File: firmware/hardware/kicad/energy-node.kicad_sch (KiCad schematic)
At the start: 14 parts, among them J1 MAINS 230V, J2 SCT-013-030 jack, J3 to Nucleo-F429ZI CN9/CN8, T1 ZMPT101B

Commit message: Update KiCad schematic and project files
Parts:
- J1: value MAINS 230V -> MAINS 230V AC
- J2: value SCT-013-030 jack -> SCT-013-030 JACK
- J3: value to Nucleo-F429ZI CN9/CN8 -> TO NUCLEO-F429ZI CN9/CN8
- R7: value 66.7 (internal) -> 66.7 internal
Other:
- note added: "1. VOLTAGE SENSING CHANNEL"
- note added: "2. CURRENT SENSING CHANNEL"
- note added: "230 V AC -> galvanic isolation and scaling -> anti-alias filter -> PA0 voltage ADC"
- note added: "3. SHARED ADC BIAS (MIDPOINT)"
- note added: "4. NUCLEO-F429ZI CONNECTIONS"
- note added: "Matching net labels connect signals without long crossing wires."
- note added: "PA0 = voltage samples; PA1 = current samples"
- note added: "Power-flag symbols are KiCad checks for supplied 3V3/GND; they are not physical parts."
- note added: "R2 converts the isolated transformer current into a measurable voltage."
- note added: "R3 and R4 make 1.65 V; C1 stabilizes it. This shifts both AC waveforms into the 0-3.3 V ADC range."
- note added: "R5 + C2 form a 1.6 kHz low-pass filter before the STM32 ADC."
- note added: "R6 + C3 match the voltage-channel filter so phase error stays aligned."
- note added: "R7 is the sensor's internal 66.7 ohm burden; do not add a second burden."
- note added: "SAFETY: J1 is mains voltage; use rated isolation, protection, and enclosure."
- note added: "SCT-013-030 clamp output -> internal burden -> anti-alias filter -> PA1 current ADC"
- note added: "V_BIAS = 1.65 V reference for both sensor channels"

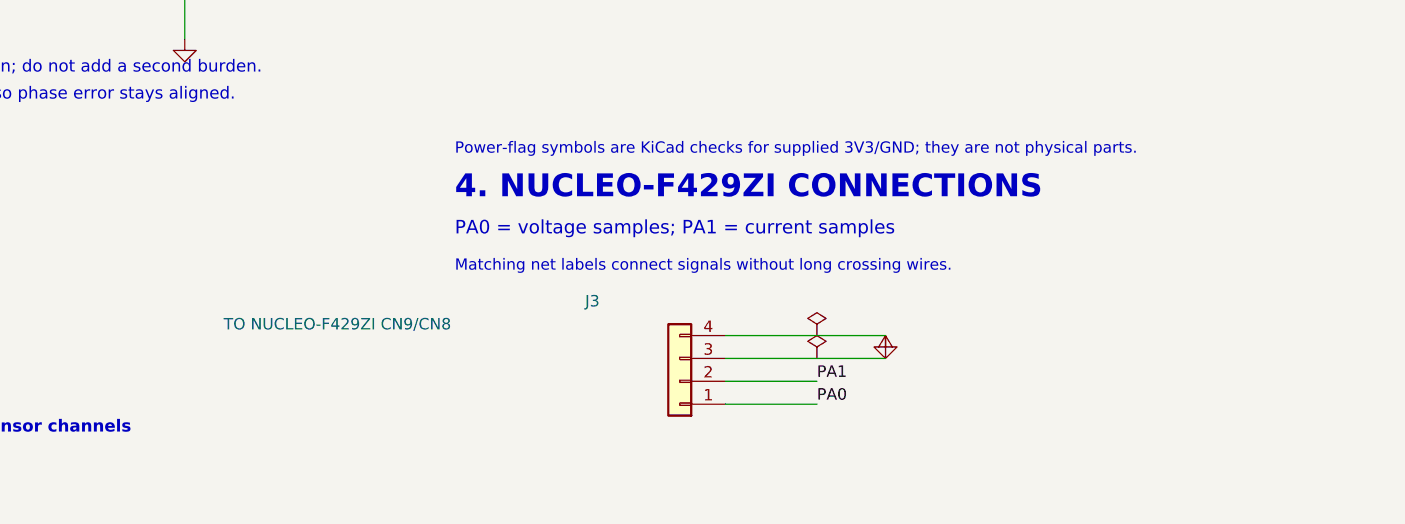
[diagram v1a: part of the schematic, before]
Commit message: Add explicit STM32 MCU model in schematic and docs
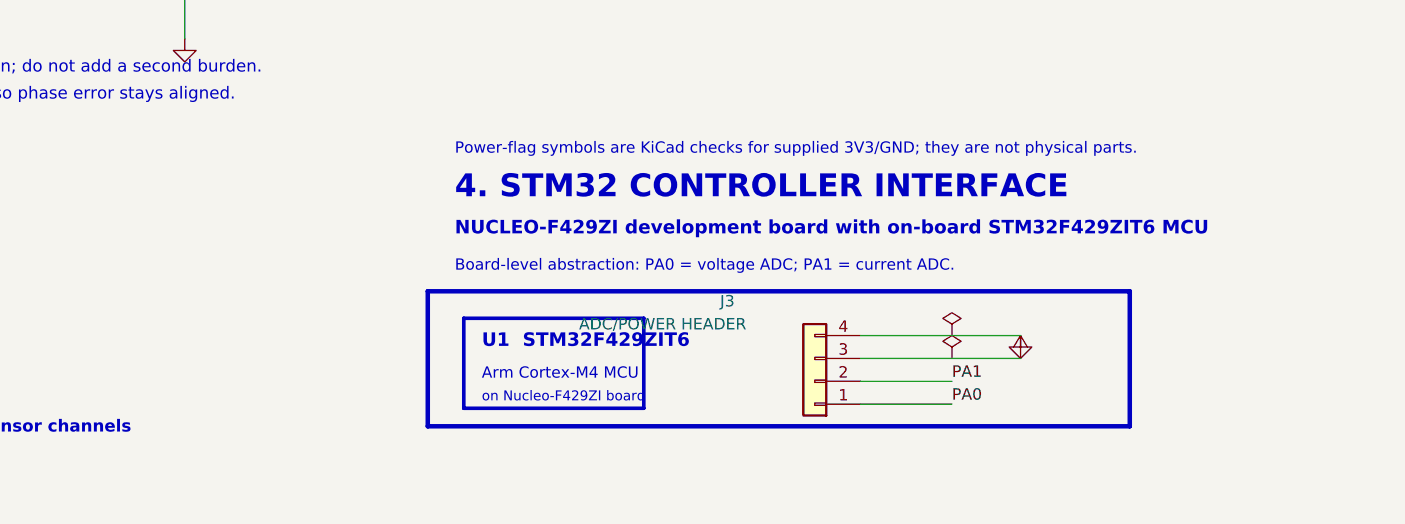
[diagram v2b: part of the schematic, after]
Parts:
- J3: value TO NUCLEO-F429ZI CN9/CN8 -> ADC/POWER HEADER
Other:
- note added: "4. STM32 CONTROLLER INTERFACE"
- note added: "Arm Cortex-M4 MCU"
- note added: "Board-level abstraction: PA0 = voltage ADC; PA1 = current ADC."
- note added: "NUCLEO-F429ZI development board with on-board STM32F429ZIT6 MCU"
- note added: "U1 STM32F429ZIT6"
- note added: "on Nucleo-F429ZI board"
- note removed: "4. NUCLEO-F429ZI CONNECTIONS"
- note removed: "Matching net labels connect signals without long crossing wires."
- note removed: "PA0 = voltage samples; PA1 = current samples"
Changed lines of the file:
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@@
   (wire (pts (xy 90 165.78) (xy 90 168.32)) (stroke (width 0) (type default)))
   (wire (pts (xy 90 158.16) (xy 110 158.16)) (stroke (width 0) (type default)))
-  (wire (pts (xy 225.08 159.54) (xy 235.24 159.54)) (stroke (width 0) (type default)))
-  (wire (pts (xy 225.08 157.0) (xy 235.24 157.0)) (stroke (width 0) (type default)))
-  (wire (pts (xy 225.08 154.46) (xy 242.86 154.46)) (stroke (width 0) (type default)))
-  (wire (pts (xy 225.08 151.92) (xy 242.86 151.92)) (stroke (width 0) (type default)))
+  (wire (pts (xy 240.08 159.54) (xy 250.24 159.54)) (stroke (width 0) (type default)))
+  (wire (pts (xy 240.08 157.0) (xy 250.24 157.0)) (stroke (width 0) (type default)))
+  (wire (pts (xy 240.08 154.46) (xy 257.86 154.46)) (stroke (width 0) (type default)))
+  (wire (pts (xy 240.08 151.92) (xy 257.86 151.92)) (stroke (width 0) (type default)))
   (label "PA0" (at 185 52.46 0) (fields_autoplaced) (effects (font (size 1.27 1.27)) (justify left bottom)))
   (junction (at 165 52.46) (diameter 0) (color 0 0 0 0))
@@
   (label "V_BIAS" (at 115.16 112.62 0) (fields_autoplaced) (effects (font (size 1.27 1.27)) (justify left bottom)))
   (label "V_BIAS" (at 110 158.16 0) (fields_autoplaced) (effects (font (size 1.27 1.27)) (justify left bottom)))
-  (label "PA0" (at 235.24 159.54 0) (fields_autoplaced) (effects (font (size 1.27 1.27)) (justify left bottom)))
-  (label "PA1" (at 235.24 157.0 0) (fields_autoplaced) (effects (font (size 1.27 1.27)) (justify left bottom)))
+  (label "PA0" (at 250.24 159.54 0) (fields_autoplaced) (effects (font (size 1.27 1.27)) (justify left bottom)))
+  (label "PA1" (at 250.24 157.0 0) (fields_autoplaced) (effects (font (size 1.27 1.27)) (justify left bottom)))
+  (rectangle (start 192 147) (end 270 162) (stroke (width 0.5) (type default)) (fill (type none)))
+  (rectangle (start 196 150) (end 216 160) (stroke (width 0.4) (type default)) (fill (type none)))
   (text "1. VOLTAGE SENSING CHANNEL" (at 25 30 0) (effects (font (size 2.54 2.54) bold) (justify left bottom)))
   (text "230 V AC -> galvanic isolation and scaling -> anti-alias filter -> PA0 voltage ADC" (at 25 34 0) (effects (font (size 1.6 1.6)) (justify left bottom)))
@@
   (text "V_BIAS = 1.65 V reference for both sensor channels" (at 105 163 0) (effects (font (size 1.35 1.35) bold) (justify left bottom)))
   (text "Power-flag symbols are KiCad checks for supplied 3V3/GND; they are not physical parts." (at 195 132 0) (effects (font (size 1.25 1.25)) (justify left bottom)))
-  (text "4. NUCLEO-F429ZI CONNECTIONS" (at 195 137 0) (effects (font (size 2.54 2.54) bold) (justify left bottom)))
-  (text "PA0 = voltage samples; PA1 = current samples" (at 195 141 0) (effects (font (size 1.5 1.5)) (justify left bottom)))
-  (text "Matching net labels connect signals without long crossing wires." (at 195 145 0) (effects (font (size 1.25 1.25)) (justify left bottom)))
+  (text "4. STM32 CONTROLLER INTERFACE" (at 195 137 0) (effects (font (size 2.54 2.54) bold) (justify left bottom)))
+  (text "NUCLEO-F429ZI development board with on-board STM32F429ZIT6 MCU" (at 195 141 0) (effects (font (size 1.5 1.5) bold) (justify left bottom)))
+  (text "Board-level abstraction: PA0 = voltage ADC; PA1 = current ADC." (at 195 145 0) (effects (font (size 1.25 1.25)) (justify left bottom)))
+  (text "U1  STM32F429ZIT6" (at 198 153.5 0) (effects (font (size 1.5 1.5) bold) (justify left bottom)))
+  (text "Arm Cortex-M4 MCU" (at 198 157 0) (effects (font (size 1.25 1.25)) (justify left bottom)))
+  (text "on Nucleo-F429ZI board" (at 198 159.5 0) (effects (font (size 1.1 1.1)) (justify left bottom)))
   (symbol (lib_id "Connector_Generic:Conn_01x02") (at 35 55 180) (unit 1)
     (in_bom yes) (on_board yes) (dnp no)
@@
       (path "/00000000-0000-0000-0000-000000000000"
         (reference "#PWR05") (unit 1)))))
-  (symbol (lib_id "Connector_Generic:Conn_01x04") (at 220 157 180) (unit 1)
-    (in_bom yes) (on_board yes) (dnp no)
-    (property "Reference" "J3" (at 211.1 148.1 0)
-      (effects (font (size 1.27 1.27)) (justify left)))
-    (property "Value" "TO NUCLEO-F429ZI CN9/CN8" (at 194.6 150.65 0)
-      (effects (font (size 1.27 1.27)) (justify left)))
-    (property "Footprint" "" (at 220 157 0) (effects (font (size 1.27 1.27)) hide))
-    (property "Datasheet" "~" (at 220 157 0) (effects (font (size 1.27 1.27)) hide))
+  (symbol (lib_id "Connector_Generic:Conn_01x04") (at 235 157 180) (unit 1)
+    (in_bom yes) (on_board yes) (dnp no)
+    (property "Reference" "J3" (at 226.1 148.1 0)
+      (effects (font (size 1.27 1.27)) (justify left)))
+    (property "Value" "ADC/POWER HEADER" (at 227.4 150.65 0)
+      (effects (font (size 1.27 1.27)) (justify left)))
+    (property "Footprint" "" (at 235 157 0) (effects (font (size 1.27 1.27)) hide))
+    (property "Datasheet" "~" (at 235 157 0) (effects (font (size 1.27 1.27)) hide))
     (pin "1")
     (pin "2")
@@
       (path "/00000000-0000-0000-0000-000000000000"
         (reference "J3") (unit 1)))))
-  (symbol (lib_id "power:+3V3") (at 242.86 154.46 0) (unit 1)
-    (in_bom yes) (on_board yes) (dnp no)
-    (property "Reference" "#PWR06" (at 245.4 154.46 0)
-      (effects (font (size 1.27 1.27)) (justify left) hide))
-    (property "Value" "+3V3" (at 245.4 157.0 0)
-      (effects (font (size 1.27 1.27)) (justify left) hide))
-    (property "Footprint" "" (at 242.86 154.46 0) (effects (font (size 1.27 1.27)) hide))
-    (property "Datasheet" "~" (at 242.86 154.46 0) (effects (font (size 1.27 1.27)) hide))
+  (symbol (lib_id "power:+3V3") (at 257.86 154.46 0) (unit 1)
+    (in_bom yes) (on_board yes) (dnp no)
+    (property "Reference" "#PWR06" (at 260.40000000000003 154.46 0)
+      (effects (font (size 1.27 1.27)) (justify left) hide))
+    (property "Value" "+3V3" (at 260.40000000000003 157.0 0)
+      (effects (font (size 1.27 1.27)) (justify left) hide))
+    (property "Footprint" "" (at 257.86 154.46 0) (effects (font (size 1.27 1.27)) hide))
+    (property "Datasheet" "~" (at 257.86 154.46 0) (effects (font (size 1.27 1.27)) hide))
     (pin "1")
     (instances (project "energy-node"
       (path "/00000000-0000-0000-0000-000000000000"
         (reference "#PWR06") (unit 1)))))
-  (symbol (lib_id "power:PWR_FLAG") (at 235.24 154.46 0) (unit 1)
-    (in_bom yes) (on_board yes) (dnp no)
-    (property "Reference" "#FLG01" (at 237.78 154.46 0)
-      (effects (font (size 1.27 1.27)) (justify left) hide))
-    (property "Value" "PWR_FLAG" (at 237.78 157.0 0)
-      (effects (font (size 1.27 1.27)) (justify left) hide))
-    (property "Footprint" "" (at 235.24 154.46 0) (effects (font (size 1.27 1.27)) hide))
-    (property "Datasheet" "~" (at 235.24 154.46 0) (effects (font (size 1.27 1.27)) hide))
+  (symbol (lib_id "power:PWR_FLAG") (at 250.24 154.46 0) (unit 1)
+    (in_bom yes) (on_board yes) (dnp no)
+    (property "Reference" "#FLG01" (at 252.78 154.46 0)
+      (effects (font (size 1.27 1.27)) (justify left) hide))
+    (property "Value" "PWR_FLAG" (at 252.78 157.0 0)
+      (effects (font (size 1.27 1.27)) (justify left) hide))
+    (property "Footprint" "" (at 250.24 154.46 0) (effects (font (size 1.27 1.27)) hide))
+    (property "Datasheet" "~" (at 250.24 154.46 0) (effects (font (size 1.27 1.27)) hide))
     (pin "1")
     (instances (project "energy-node"
       (path "/00000000-0000-0000-0000-000000000000"
         (reference "#FLG01") (unit 1)))))
-  (symbol (lib_id "power:GND") (at 242.86 151.92 0) (unit 1)
-    (in_bom yes) (on_board yes) (dnp no)
-    (property "Reference" "#PWR07" (at 245.4 151.92 0)
-      (effects (font (size 1.27 1.27)) (justify left) hide))
-    (property "Value" "GND" (at 245.4 154.45999999999998 0)
-      (effects (font (size 1.27 1.27)) (justify left) hide))
-    (property "Footprint" "" (at 242.86 151.92 0) (effects (font (size 1.27 1.27)) hide))
-    (property "Datasheet" "~" (at 242.86 151.92 0) (effects (font (size 1.27 1.27)) hide))
+  (symbol (lib_id "power:GND") (at 257.86 151.92 0) (unit 1)
+    (in_bom yes) (on_board yes) (dnp no)
+    (property "Reference" "#PWR07" (at 260.40000000000003 151.92 0)
+      (effects (font (size 1.27 1.27)) (justify left) hide))
+    (property "Value" "GND" (at 260.40000000000003 154.45999999999998 0)
+      (effects (font (size 1.27 1.27)) (justify left) hide))
+    (property "Footprint" "" (at 257.86 151.92 0) (effects (font (size 1.27 1.27)) hide))
+    (property "Datasheet" "~" (at 257.86 151.92 0) (effects (font (size 1.27 1.27)) hide))
     (pin "1")
     (instances (project "energy-node"
       (path "/00000000-0000-0000-0000-000000000000"
         (reference "#PWR07") (unit 1)))))
-  (symbol (lib_id "power:PWR_FLAG") (at 235.24 151.92 0) (unit 1)
-    (in_bom yes) (on_board yes) (dnp no)
-    (property "Reference" "#FLG02" (at 237.78 151.92 0)
-      (effects (font (size 1.27 1.27)) (justify left) hide))
-    (property "Value" "PWR_FLAG" (at 237.78 154.45999999999998 0)
-      (effects (font (size 1.27 1.27)) (justify left) hide))
-    (property "Footprint" "" (at 235.24 151.92 0) (effects (font (size 1.27 1.27)) hide))
-    (property "Datasheet" "~" (at 235.24 151.92 0) (effects (font (size 1.27 1.27)) hide))
-    (pin "1")
-    (instances (project "energy-node"
+  (symbol (lib_id "power:PWR_FLAG") (at 250.24 151.92 0) (unit 1)
+    (in_bom yes) (on_board yes) (dnp no)
+    (property "Reference" "#FLG02" (at 252.78 151.92 0)
+      (effects (font (size 1.27 1.27)) (justify left) hide))
+    (property "Value" "PWR_FLAG" (at 252.78 154.45999999999998 0)
+      (effects (font (size 1.27 1.27)) (justify left) hide))
+    (property "Footprint" "" (at 250.24 151.92 0) (effects (font (size 1.27 1.27)) hide))
+    (property "Datasheet" "~" (at 250.24 151.92 0) (effects (font (size 1.27 1.27)) hide))
+    (pin "1")
+    (instances (project "energy-node"
